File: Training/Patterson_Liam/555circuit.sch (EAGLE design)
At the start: 6 parts, among them IC1 LM555D

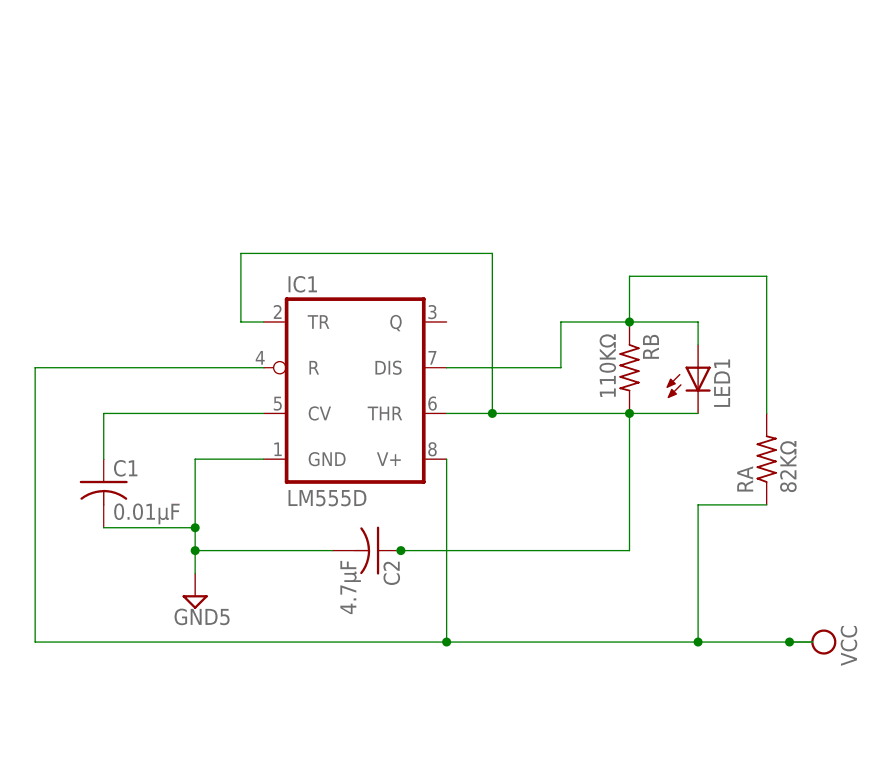
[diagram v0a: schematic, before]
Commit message: Hopefully made the schematic a little easier to read.
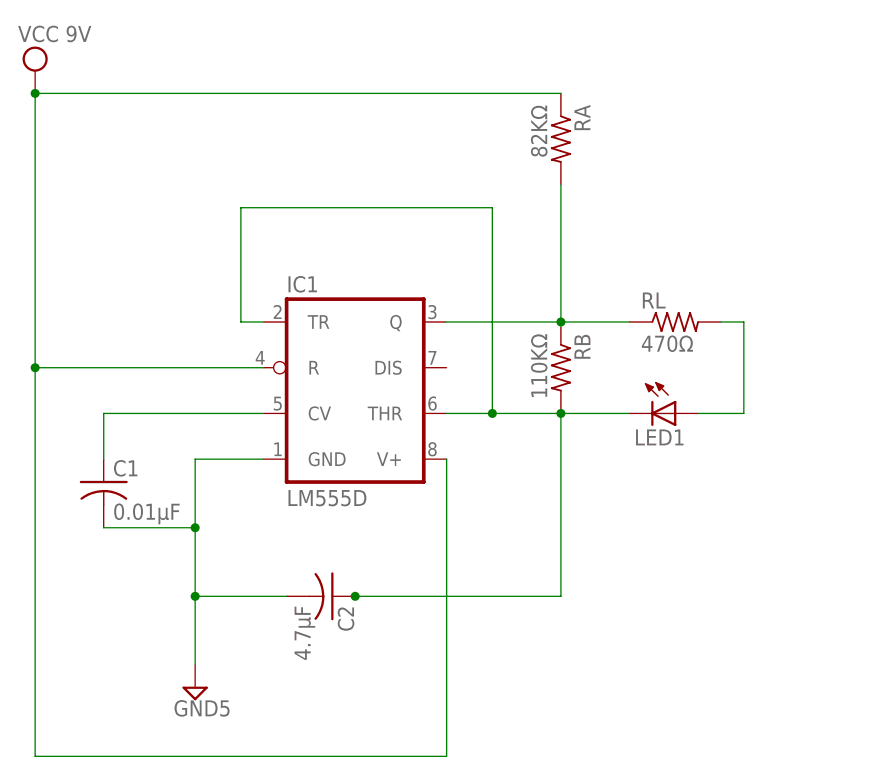
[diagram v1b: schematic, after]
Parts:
- added RL: 470Ω, resistor:R-US_0204/2V
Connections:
- new net N$2: LED1.A, RL.2
- net N$5: now also IC1.Q, RL.1; no longer IC1.DIS, LED1.A
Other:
- moved on the sheet: C2, LED1, RA, RB
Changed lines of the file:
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@@
 <part name="LED1" library="led" deviceset="LED" device=""/>
 <part name="C2" library="resistor" deviceset="C-US" device="025-024X044" value="4.7μF"/>
-<part name="SUPPLY2" library="supply2" deviceset="VCC" device=""/>
+<part name="SUPPLY2" library="supply2" deviceset="VCC" device="" value="VCC 9V"/>
+<part name="RL" library="resistor" deviceset="R-US_" device="0204/2V" value="470Ω"/>
 </parts>
 <sheets>
@@
 <instances>
 <instance part="IC1" gate="A" x="66.04" y="68.58"/>
-<instance part="SUPPLY1" gate="G$1" x="48.26" y="45.72"/>
+<instance part="SUPPLY1" gate="G$1" x="48.26" y="35.56"/>
 <instance part="C1" gate="G$1" x="38.1" y="58.42"/>
-<instance part="RB" gate="G$1" x="96.52" y="71.12" rot="R270"/>
-<instance part="RA" gate="G$1" x="111.76" y="60.96" rot="R90"/>
-<instance part="LED1" gate="G$1" x="104.14" y="71.12"/>
-<instance part="C2" gate="G$1" x="68.58" y="50.8" rot="R270"/>
-<instance part="SUPPLY2" gate="G$1" x="116.84" y="40.64" rot="R270"/>
+<instance part="RB" gate="G$1" x="88.9" y="71.12" rot="R270"/>
+<instance part="RA" gate="G$1" x="88.9" y="96.52" rot="R270"/>
+<instance part="LED1" gate="G$1" x="101.6" y="66.04" rot="R270"/>
+<instance part="C2" gate="G$1" x="63.5" y="45.72" rot="R270"/>
+<instance part="SUPPLY2" gate="G$1" x="30.48" y="104.14"/>
+<instance part="RL" gate="G$1" x="101.6" y="76.2"/>
 </instances>
 <busses>
@@
 <wire x1="48.26" y1="60.96" x2="48.26" y2="53.34" width="0.1524" layer="91"/>
 <pinref part="C1" gate="G$1" pin="2"/>
-<wire x1="48.26" y1="53.34" x2="48.26" y2="50.8" width="0.1524" layer="91"/>
-<wire x1="48.26" y1="50.8" x2="48.26" y2="48.26" width="0.1524" layer="91"/>
+<wire x1="48.26" y1="53.34" x2="48.26" y2="45.72" width="0.1524" layer="91"/>
+<wire x1="48.26" y1="45.72" x2="48.26" y2="38.1" width="0.1524" layer="91"/>
 <wire x1="38.1" y1="53.34" x2="48.26" y2="53.34" width="0.1524" layer="91"/>
 <junction x="48.26" y="53.34"/>
 <pinref part="C2" gate="G$1" pin="2"/>
-<wire x1="63.5" y1="50.8" x2="48.26" y2="50.8" width="0.1524" layer="91"/>
-<junction x="48.26" y="50.8"/>
+<wire x1="58.42" y1="45.72" x2="48.26" y2="45.72" width="0.1524" layer="91"/>
+<junction x="48.26" y="45.72"/>
 </segment>
 </net>
@@
 <segment>
 <pinref part="SUPPLY2" gate="G$1" pin="VCC"/>
-<wire x1="114.3" y1="40.64" x2="116.84" y2="40.64" width="0.1524" layer="91"/>
+<pinref part="RA" gate="G$1" pin="1"/>
+<wire x1="30.48" y1="101.6" x2="88.9" y2="101.6" width="0.1524" layer="91"/>
 <pinref part="IC1" gate="A" pin="R"/>
 <wire x1="55.88" y1="71.12" x2="30.48" y2="71.12" width="0.1524" layer="91"/>
-<wire x1="30.48" y1="71.12" x2="30.48" y2="40.64" width="0.1524" layer="91"/>
-<wire x1="30.48" y1="40.64" x2="76.2" y2="40.64" width="0.1524" layer="91"/>
+<wire x1="30.48" y1="71.12" x2="30.48" y2="27.94" width="0.1524" layer="91"/>
+<wire x1="30.48" y1="27.94" x2="76.2" y2="27.94" width="0.1524" layer="91"/>
 <pinref part="IC1" gate="A" pin="V+"/>
-<wire x1="76.2" y1="60.96" x2="76.2" y2="40.64" width="0.1524" layer="91"/>
-<wire x1="76.2" y1="40.64" x2="104.14" y2="40.64" width="0.1524" layer="91"/>
-<junction x="76.2" y="40.64"/>
-<junction x="114.3" y="40.64"/>
-<pinref part="RA" gate="G$1" pin="1"/>
-<wire x1="104.14" y1="40.64" x2="114.3" y2="40.64" width="0.1524" layer="91"/>
-<wire x1="104.14" y1="40.64" x2="104.14" y2="55.88" width="0.1524" layer="91"/>
-<wire x1="104.14" y1="55.88" x2="111.76" y2="55.88" width="0.1524" layer="91"/>
-<junction x="104.14" y="40.64"/>
-</segment>
-</net>
-<net name="N$3" class="0">
-<segment>
-<pinref part="C2" gate="G$1" pin="1"/>
-<wire x1="71.12" y1="50.8" x2="96.52" y2="50.8" width="0.1524" layer="91"/>
-<junction x="71.12" y="50.8"/>
-<pinref part="IC1" gate="A" pin="THR"/>
-<pinref part="LED1" gate="G$1" pin="C"/>
-<wire x1="76.2" y1="66.04" x2="81.28" y2="66.04" width="0.1524" layer="91"/>
-<wire x1="81.28" y1="66.04" x2="96.52" y2="66.04" width="0.1524" layer="91"/>
-<wire x1="96.52" y1="66.04" x2="104.14" y2="66.04" width="0.1524" layer="91"/>
-<wire x1="81.28" y1="66.04" x2="81.28" y2="83.82" width="0.1524" layer="91"/>
-<junction x="81.28" y="66.04"/>
-<wire x1="81.28" y1="83.82" x2="53.34" y2="83.82" width="0.1524" layer="91"/>
-<pinref part="IC1" gate="A" pin="TR"/>
-<wire x1="53.34" y1="83.82" x2="53.34" y2="76.2" width="0.1524" layer="91"/>
-<wire x1="53.34" y1="76.2" x2="55.88" y2="76.2" width="0.1524" layer="91"/>
-<pinref part="RB" gate="G$1" pin="2"/>
-<junction x="96.52" y="66.04"/>
-<wire x1="96.52" y1="50.8" x2="96.52" y2="66.04" width="0.1524" layer="91"/>
+<wire x1="76.2" y1="60.96" x2="76.2" y2="27.94" width="0.1524" layer="91"/>
+<wire x1="30.48" y1="71.12" x2="30.48" y2="101.6" width="0.1524" layer="91"/>
+<junction x="30.48" y="101.6"/>
+<junction x="30.48" y="71.12"/>
 </segment>
 </net>
 <net name="N$5" class="0">
 <segment>
-<pinref part="LED1" gate="G$1" pin="A"/>
-<wire x1="104.14" y1="76.2" x2="104.14" y2="73.66" width="0.1524" layer="91"/>
 <pinref part="RB" gate="G$1" pin="1"/>
-<wire x1="96.52" y1="76.2" x2="104.14" y2="76.2" width="0.1524" layer="91"/>
-<junction x="96.52" y="76.2"/>
+<junction x="88.9" y="76.2"/>
+<pinref part="RA" gate="G$1" pin="2"/>
+<wire x1="88.9" y1="91.44" x2="88.9" y2="76.2" width="0.1524" layer="91"/>
+<pinref part="IC1" gate="A" pin="Q"/>
+<wire x1="76.2" y1="76.2" x2="88.9" y2="76.2" width="0.1524" layer="91"/>
+<pinref part="RL" gate="G$1" pin="1"/>
 <wire x1="88.9" y1="76.2" x2="96.52" y2="76.2" width="0.1524" layer="91"/>
-<wire x1="88.9" y1="71.12" x2="88.9" y2="76.2" width="0.1524" layer="91"/>
-<pinref part="IC1" gate="A" pin="DIS"/>
-<wire x1="76.2" y1="71.12" x2="88.9" y2="71.12" width="0.1524" layer="91"/>
-<pinref part="RA" gate="G$1" pin="2"/>
-<wire x1="111.76" y1="66.04" x2="111.76" y2="81.28" width="0.1524" layer="91"/>
-<wire x1="111.76" y1="81.28" x2="96.52" y2="81.28" width="0.1524" layer="91"/>
-<wire x1="96.52" y1="81.28" x2="96.52" y2="76.2" width="0.1524" layer="91"/>
 </segment>
 </net>
+<net name="N$1" class="0">
+<segment>
+<pinref part="IC1" gate="A" pin="TR"/>
+<wire x1="53.34" y1="76.2" x2="55.88" y2="76.2" width="0.1524" layer="91"/>
+<wire x1="53.34" y1="76.2" x2="53.34" y2="88.9" width="0.1524" layer="91"/>
+<wire x1="53.34" y1="88.9" x2="81.28" y2="88.9" width="0.1524" layer="91"/>
+<pinref part="C2" gate="G$1" pin="1"/>
+<wire x1="66.04" y1="45.72" x2="88.9" y2="45.72" width="0.1524" layer="91"/>
+<junction x="66.04" y="45.72"/>
+<pinref part="IC1" gate="A" pin="THR"/>
+<wire x1="76.2" y1="66.04" x2="81.28" y2="66.04" width="0.1524" layer="91"/>
+<pinref part="RB" gate="G$1" pin="2"/>
+<junction x="88.9" y="66.04"/>
+<wire x1="81.28" y1="66.04" x2="88.9" y2="66.04" width="0.1524" layer="91"/>
+<wire x1="88.9" y1="45.72" x2="88.9" y2="66.04" width="0.1524" layer="91"/>
+<pinref part="LED1" gate="G$1" pin="C"/>
+<wire x1="96.52" y1="66.04" x2="88.9" y2="66.04" width="0.1524" layer="91"/>
+<wire x1="81.28" y1="88.9" x2="81.28" y2="66.04" width="0.1524" layer="91"/>
+<junction x="81.28" y="66.04"/>
+</segment>
+</net>
+<net name="N$2" class="0">
+<segment>
+<pinref part="RL" gate="G$1" pin="2"/>
+<wire x1="106.68" y1="76.2" x2="109.22" y2="76.2" width="0.1524" layer="91"/>
+<wire x1="109.22" y1="76.2" x2="109.22" y2="66.04" width="0.1524" layer="91"/>
+<pinref part="LED1" gate="G$1" pin="A"/>
+<wire x1="109.22" y1="66.04" x2="104.14" y2="66.04" width="0.1524" layer="91"/>
+</segment>
+</net>
